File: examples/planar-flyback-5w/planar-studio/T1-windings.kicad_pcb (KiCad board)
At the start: 6 copper layers, 36.9 x 44.5 mm, 0 parts

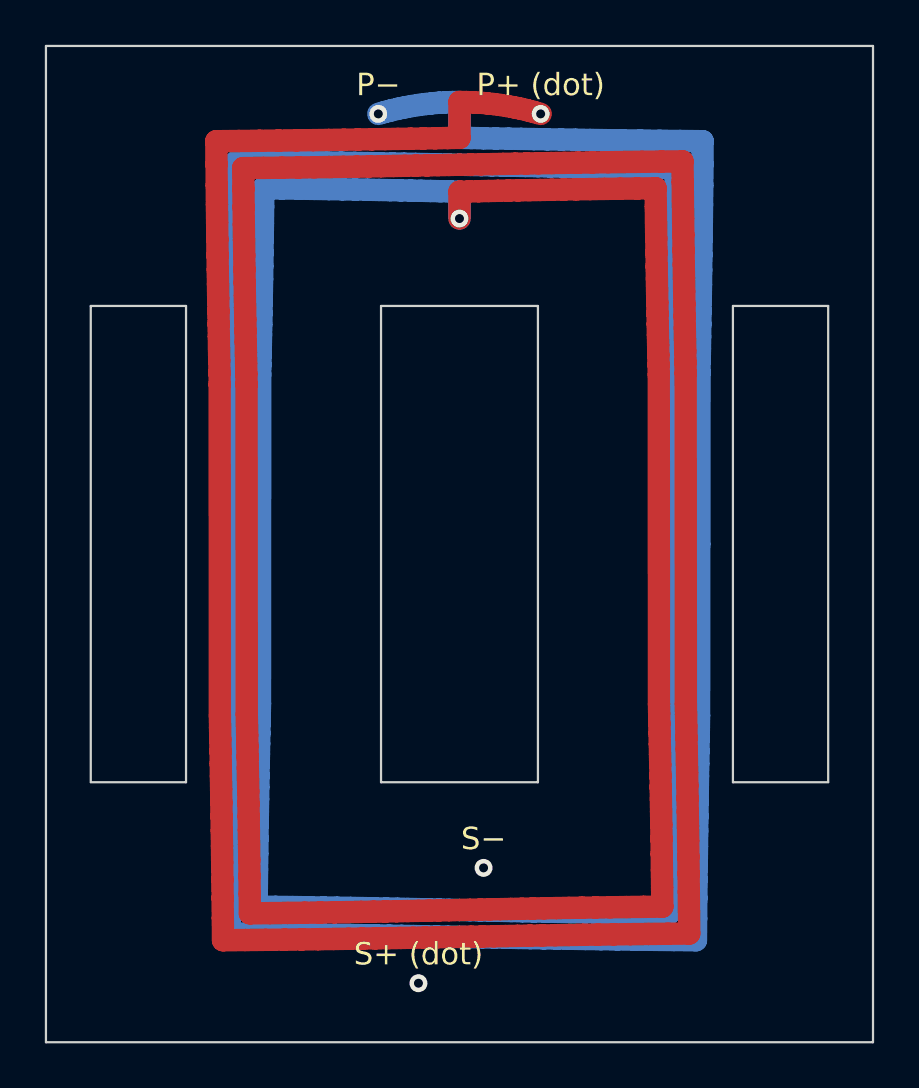
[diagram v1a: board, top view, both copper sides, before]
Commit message: Add flyback A2 with stocked factory-gapped ELP22 cores
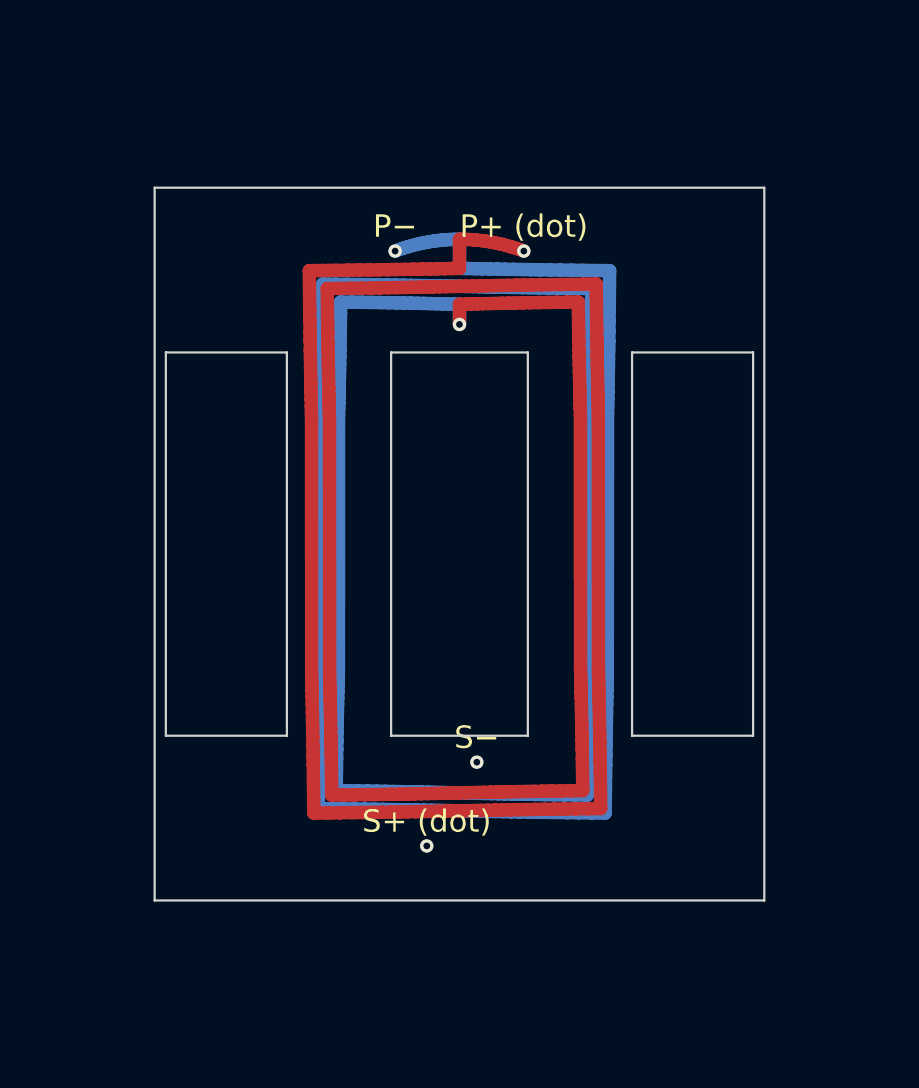
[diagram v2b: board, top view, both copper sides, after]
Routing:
- net T1_PRI: track 440.6 -> 290.3 mm
- net T1_SEC: track 439.1 -> 288.9 mm
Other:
- board size 36.9 x 44.5 mm -> 27.2 x 31.8 mm

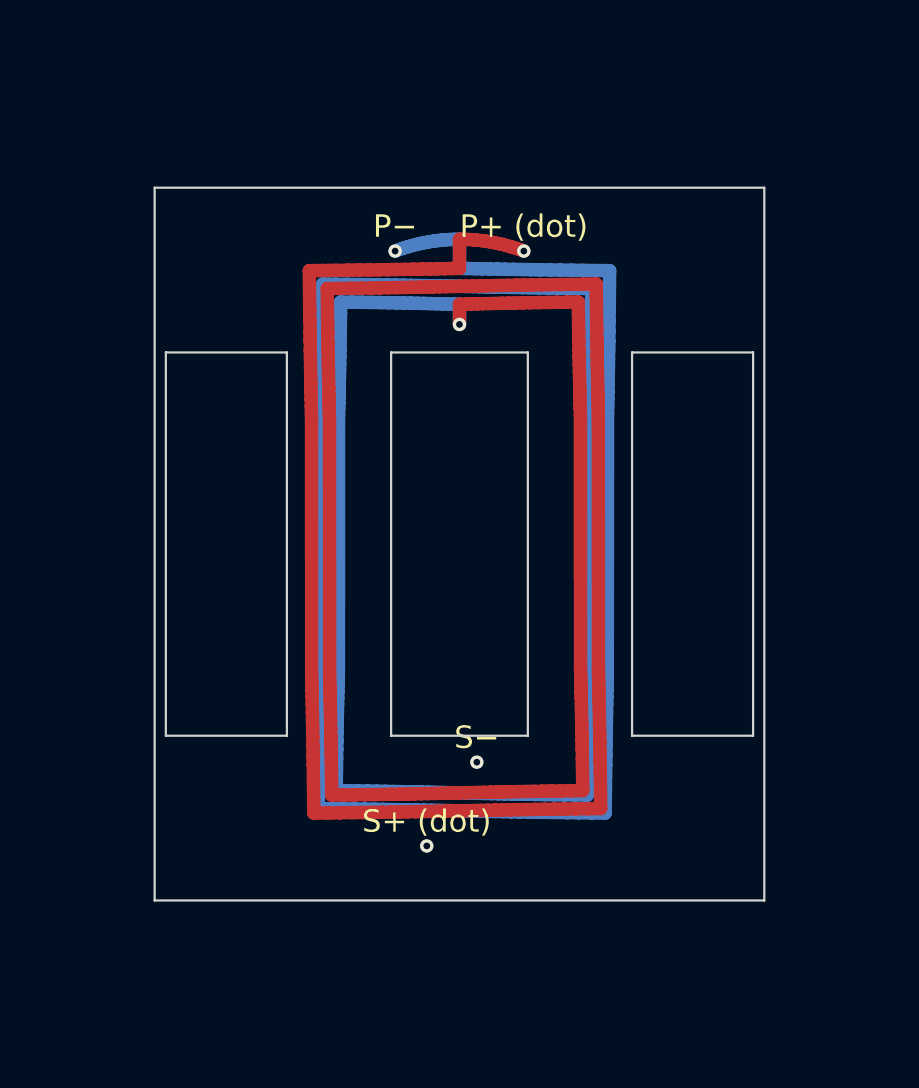
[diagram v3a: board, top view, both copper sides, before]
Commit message: Fix flyback turn spacing and document PCB integration pitfalls
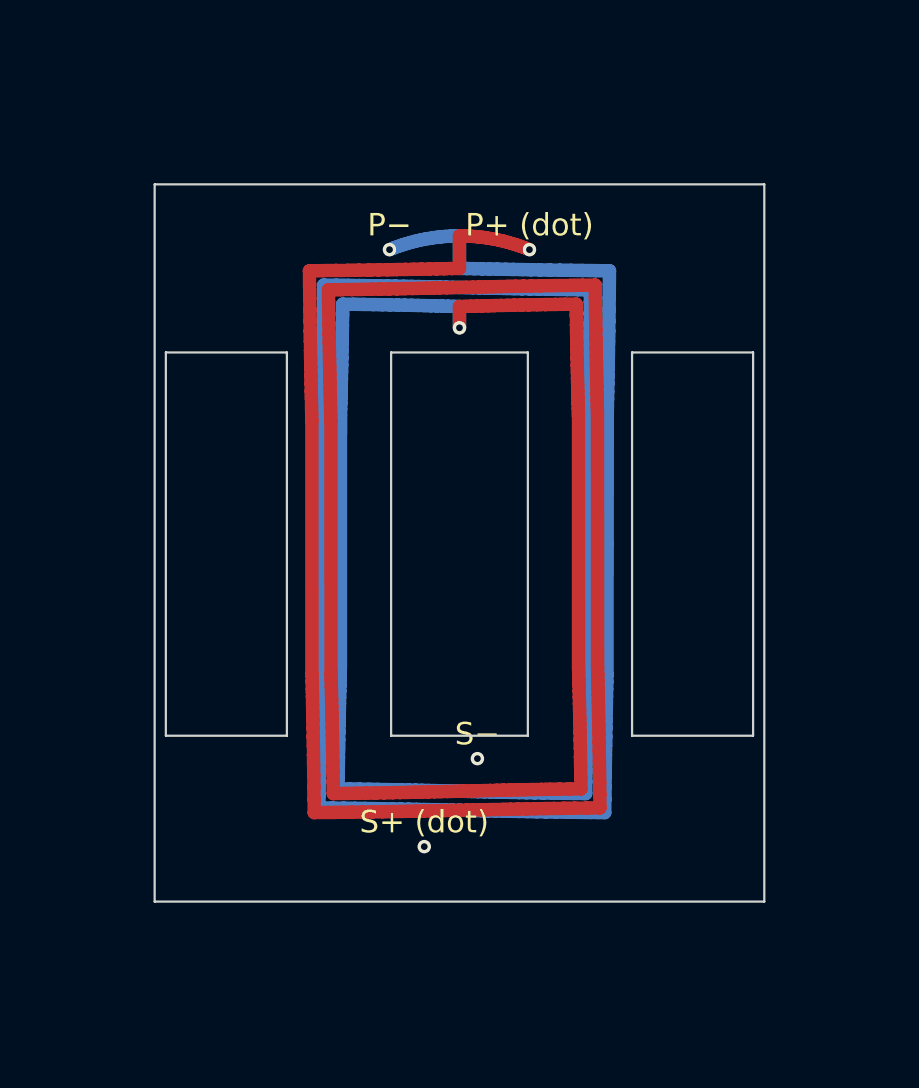
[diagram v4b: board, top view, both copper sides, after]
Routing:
- net T1_SEC: track 288.9 -> 287.8 mm
- net T1_PRI: track 290.3 -> 289.6 mm
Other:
- board size 27.2 x 31.8 mm -> 27.2 x 32 mm

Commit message: Fix flyback winding and via clearances in A10
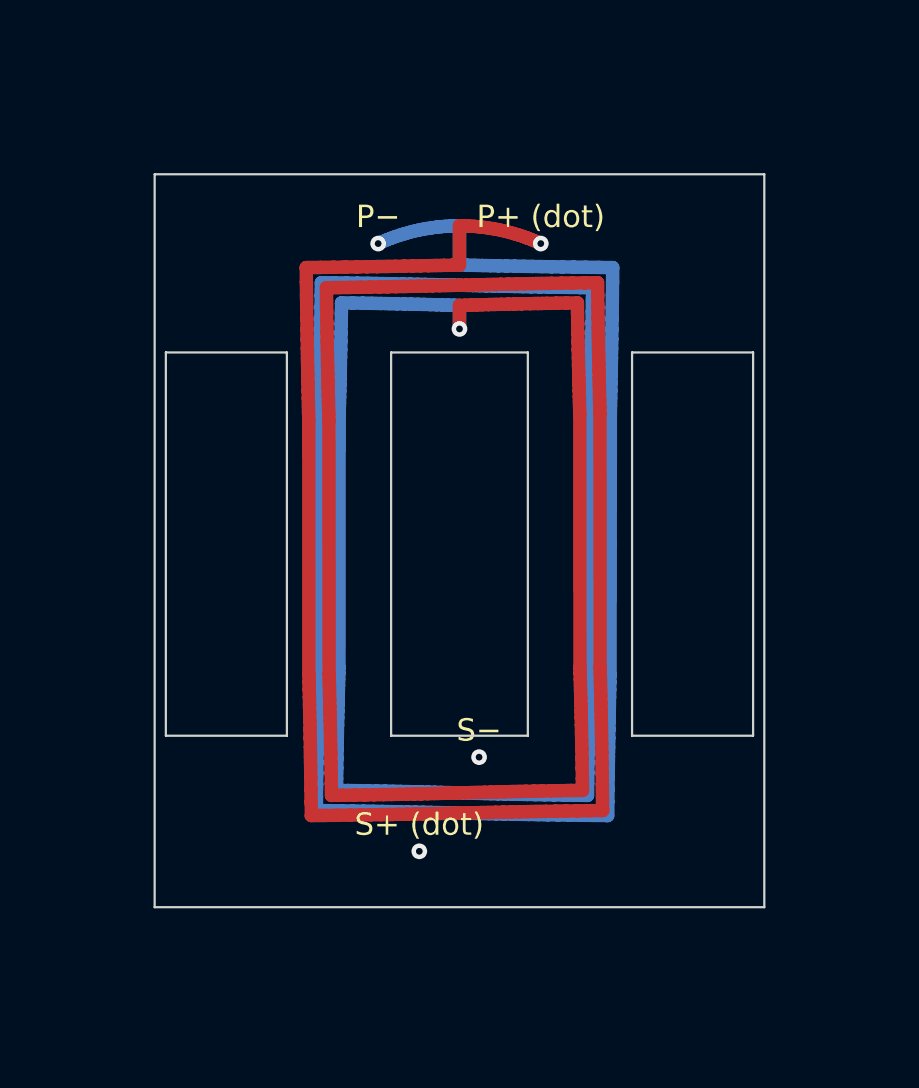
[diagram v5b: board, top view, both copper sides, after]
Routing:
- net T1_PRI: track 289.6 -> 294.7 mm
- net T1_SEC: track 287.8 -> 292.0 mm
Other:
- board size 27.2 x 32 mm -> 27.2 x 32.7 mm
